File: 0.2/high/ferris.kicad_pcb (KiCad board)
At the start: 2 copper layers, 219.1 x 95.2 mm, 109 parts, among them J1 TYPE-C-31-M-12, K0_0 KEYSW, K0_1 KEYSW, K0_2 KEYSW, K0_3 KEYSW, K0_4 KEYSW, K0_5 KEYSW, K0_6 KEYSW, K0_7 KEYSW, K0_8 KEYSW, K0_9 KEYSW, K1_0 KEYSW, K1_1 KEYSW, K1_2 KEYSW, K1_3 KEYSW, K1_4 KEYSW, K1_5 KEYSW, K1_6 KEYSW, K1_7 KEYSW, K1_8 KEYSW, K1_9 KEYSW, K2_0 KEYSW, K2_1 KEYSW, K2_2 KEYSW, K2_3 KEYSW, K2_4 KEYSW, K2_5 KEYSW, K2_6 KEYSW, K2_7 KEYSW, K2_8 KEYSW, K2_9 KEYSW, K3_3 KEYSW, K3_4 KEYSW, K3_5 KEYSW, K3_6 KEYSW, Q1 PDTC123JT,215, SW1 B3U-1000P, U1 STM32F072CBT6, U2 MCP23017-E/SO, U3 MCP1700T-3302E/TT, U4 SRV05-4

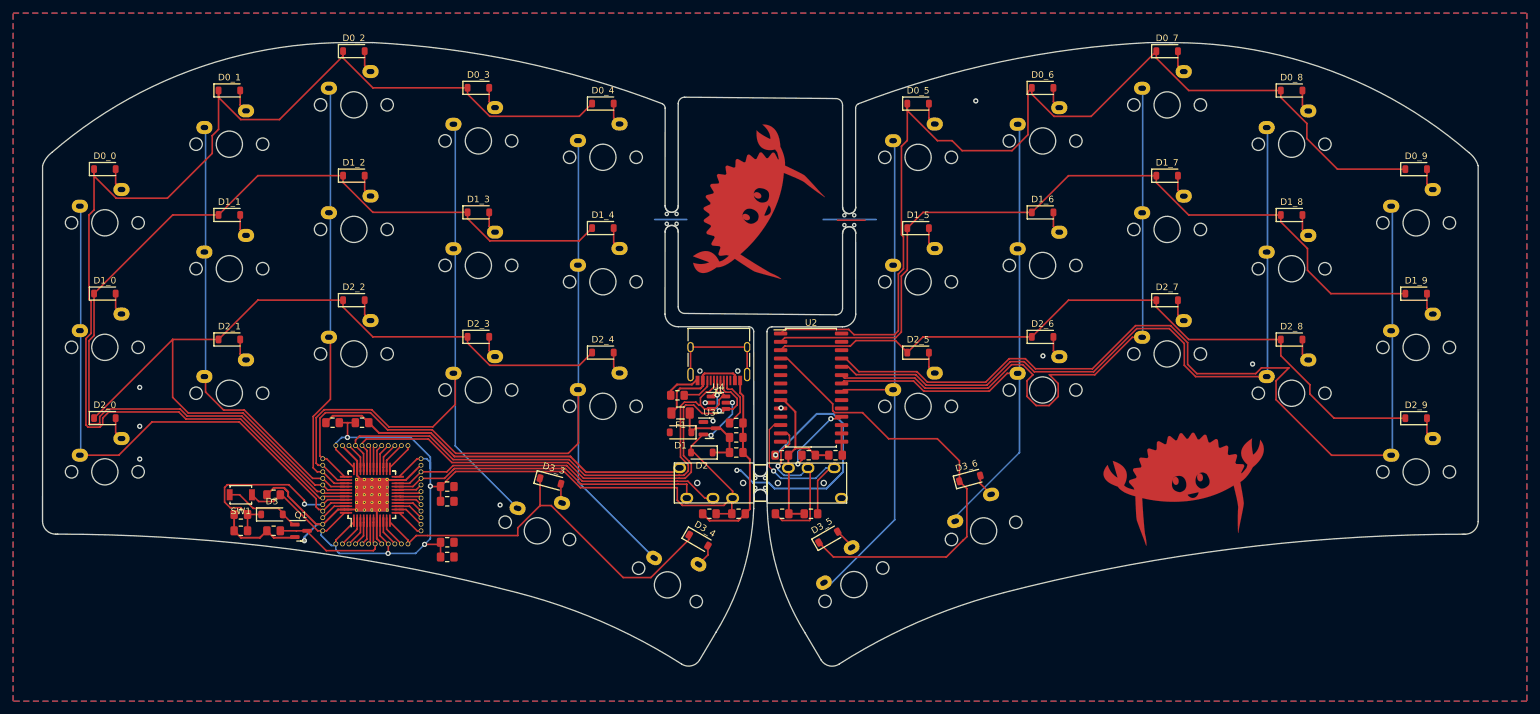
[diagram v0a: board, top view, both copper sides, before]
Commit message: Strip down board
Fix a couple of 3D models

Should do this for the complete board
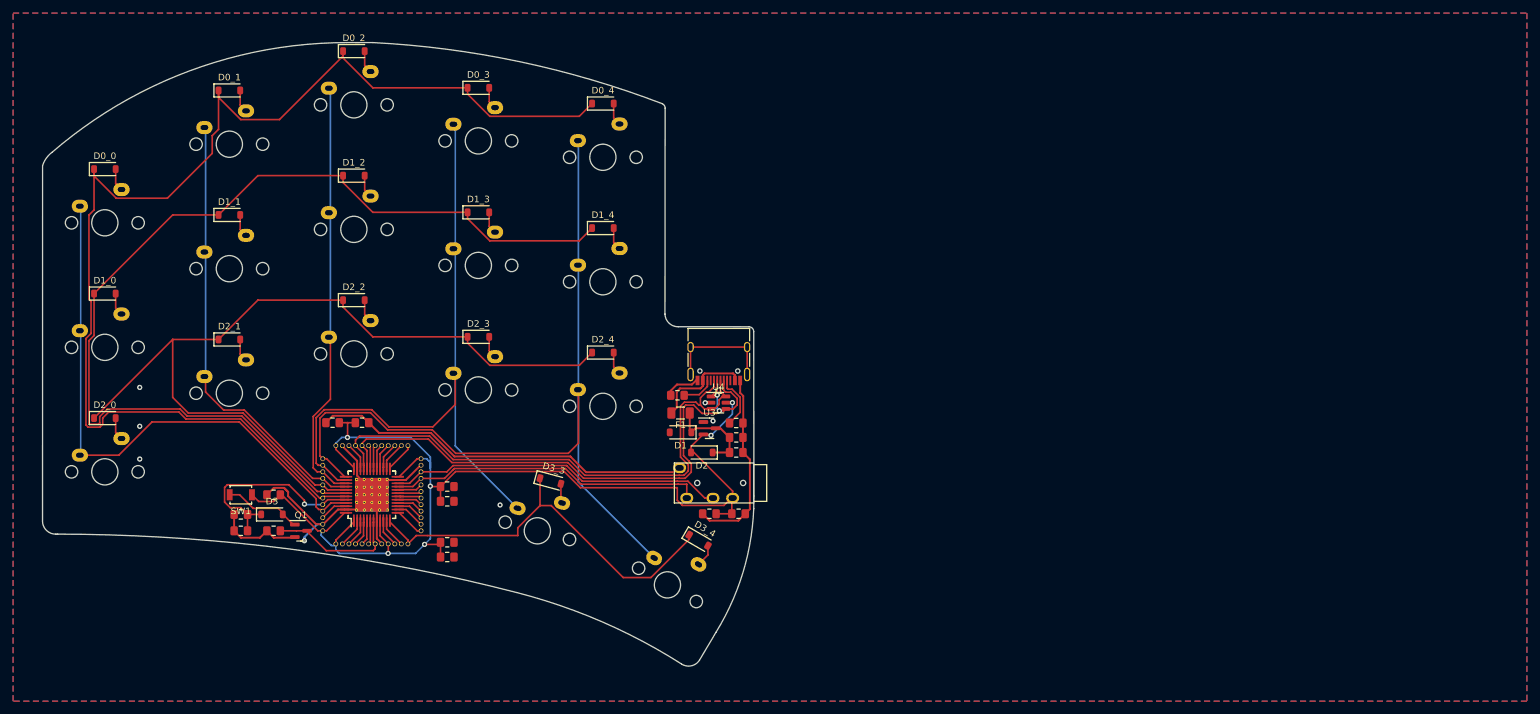
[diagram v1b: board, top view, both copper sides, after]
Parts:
- removed C12, C13: 0.1uF, Capacitor_SMD:C_0805_2012Metric_Pad1.15x1.40mm_HandSolder
- removed D0_5, D0_6, D0_7, D0_8, D0_9, D1_5, D1_6, D1_7, D1_8, D1_9, D2_5, D2_6, D2_7, D2_8, D2_9, D3_5, D3_6: 1N4148W, Diode_SMD:D_SOD-123
- removed the G*** at (189.2, 82.1)
- removed the G*** at (123.5, 40.1)
- removed the G*** at (183.5, 51.0)
- removed Jack1: PJ-320A, kbd:TRRS-PJ-320A
- removed K0_5, K0_6, K0_7, K0_8, K0_9, K1_5, K1_6, K1_7, K1_8, K1_9, K2_5, K2_6, K2_7, K2_8, K2_9, K3_5, K3_6: KEYSW, switches:MX
- removed R6: 10kΩ, Resistor_SMD:R_0805_2012Metric_Pad1.15x1.40mm_HandSolder
- removed R7, R8: 4.7kΩ, Resistor_SMD:R_0805_2012Metric_Pad1.15x1.40mm_HandSolder
- removed REF** (x3): mouse-bite-2mm-slot-with-space-for-track, panelization:mouse-bite-2mm-slot-with-space-for-track
- removed U2: MCP23017-E/SO, Package_SO:SOIC-28W_7.5x17.9mm_P1.27mm
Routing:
- net /row1,0: track 158.2 -> 0.00 mm
- net /col9: track 145.0 -> 0.00 mm
- net /row1,1: track 125.2 -> 0.00 mm
- net /col8: track 114.1 -> 0.00 mm
- net /row1,2: track 110.4 -> 0.00 mm
- net /col7: track 100.3 -> 0.00 mm
- net /col6: track 94.0 -> 0.00 mm
- net /col5: track 81.1 -> 0.00 mm
- net /row1,3: track 71.2 -> 0.00 mm
- net GND: track 220.0 -> 158.8 mm, vias 13 -> 7
- net i2c_scl_right: track 27.4 -> 0.00 mm, vias 1 -> 0
- net VDD: track 26.9 -> 0.00 mm
- net i2c_sda_right: track 26.8 -> 0.00 mm, vias 1 -> 0
- net Net-(U2-~{RESET}): track 12.3 -> 0.00 mm, vias 2 -> 0
- net Net-(D3_6-A): track 3.54 -> 0.00 mm
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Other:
- board size 219.1 x 95.2 mm -> 108.5 x 95.2 mm
- board text removed: "Ferris High - v0.2 by @pierrec83 It's just a keyboard :) * Split, 34 keys * MX switches * Microcontroller: STM32F072 * IO expander: MCP23017 * USB C * Dimensions: 96*108mm per side * All MCU pins are broken out Fully open-source design: GitHub: pierrechevalier83/ferris"
- board text removed: "Ferris High v0.2"

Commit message: Successfully routed reversible MX footprints
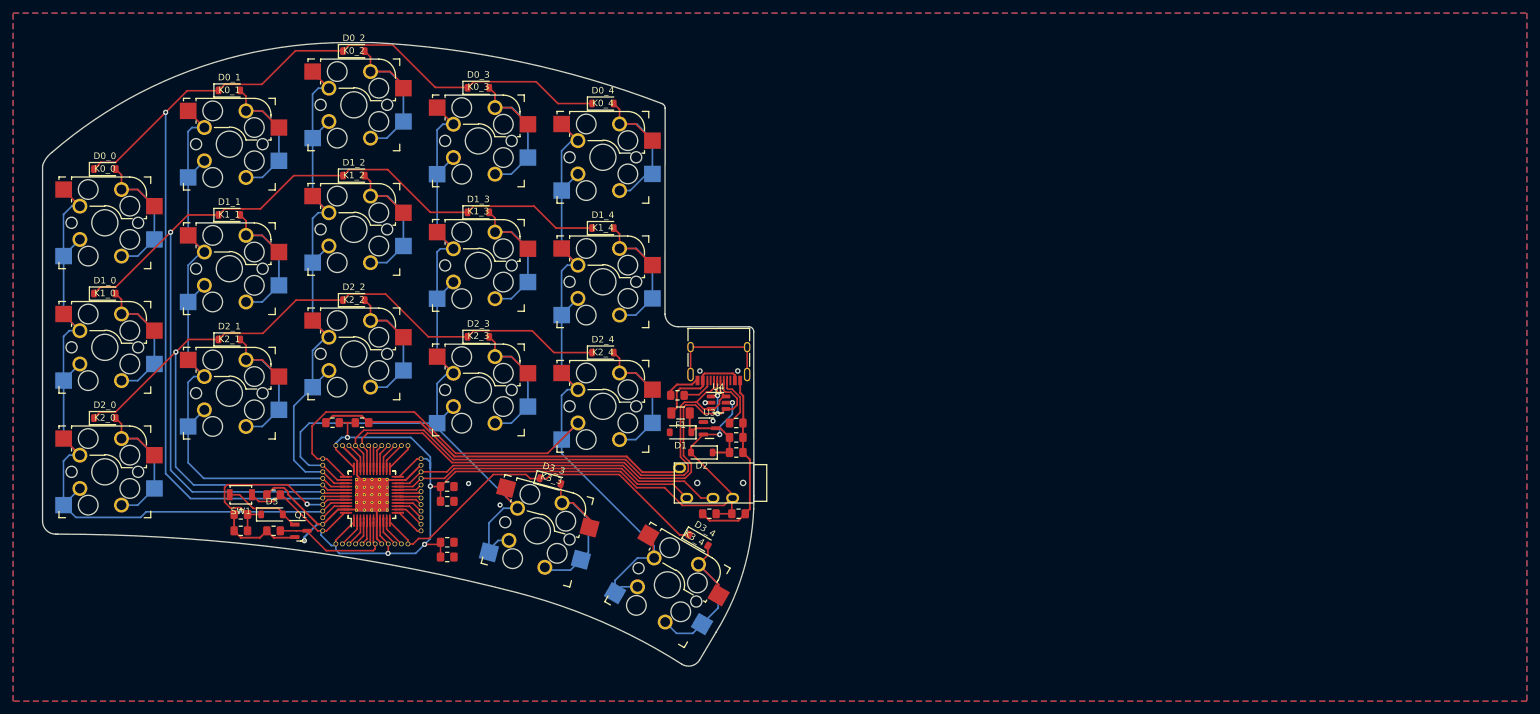
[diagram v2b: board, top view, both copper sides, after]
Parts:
- K0_0, K0_1, K0_2, K0_3, K0_4, K1_0, K1_1, K1_2, K1_3, K1_4, K2_0, K2_1, K2_2, K2_3, K2_4, K3_3, K3_4: footprint switches:MX -> daprice_keyswitches:Kailh_socket_MX_optional_reversible
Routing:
- net /col4: track 130.7 -> 171.2 mm
- net /col3: track 104.3 -> 144.0 mm
- net /col1: track 67.7 -> 105.4 mm
- net /col0: track 87.2 -> 119.4 mm
- net /col2: track 65.0 -> 95.9 mm
- net Net-(D3_3-A): track 3.00 -> 27.6 mm
- net Net-(D3_4-A): track 3.44 -> 27.7 mm
- net Net-(D0_4-A): track 3.49 -> 26.9 mm
- net Net-(D0_3-A): track 3.39 -> 26.8 mm
- net Net-(D1_2-A): track 3.49 -> 26.8 mm
- net Net-(D1_4-A): track 3.49 -> 26.8 mm
- net Net-(D1_3-A): track 3.39 -> 26.7 mm
- net Net-(D2_2-A): track 3.49 -> 26.8 mm
- net Net-(D0_2-A): track 3.49 -> 26.8 mm
- net Net-(D2_4-A): track 3.49 -> 26.8 mm
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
